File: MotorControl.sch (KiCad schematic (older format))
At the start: 0 parts

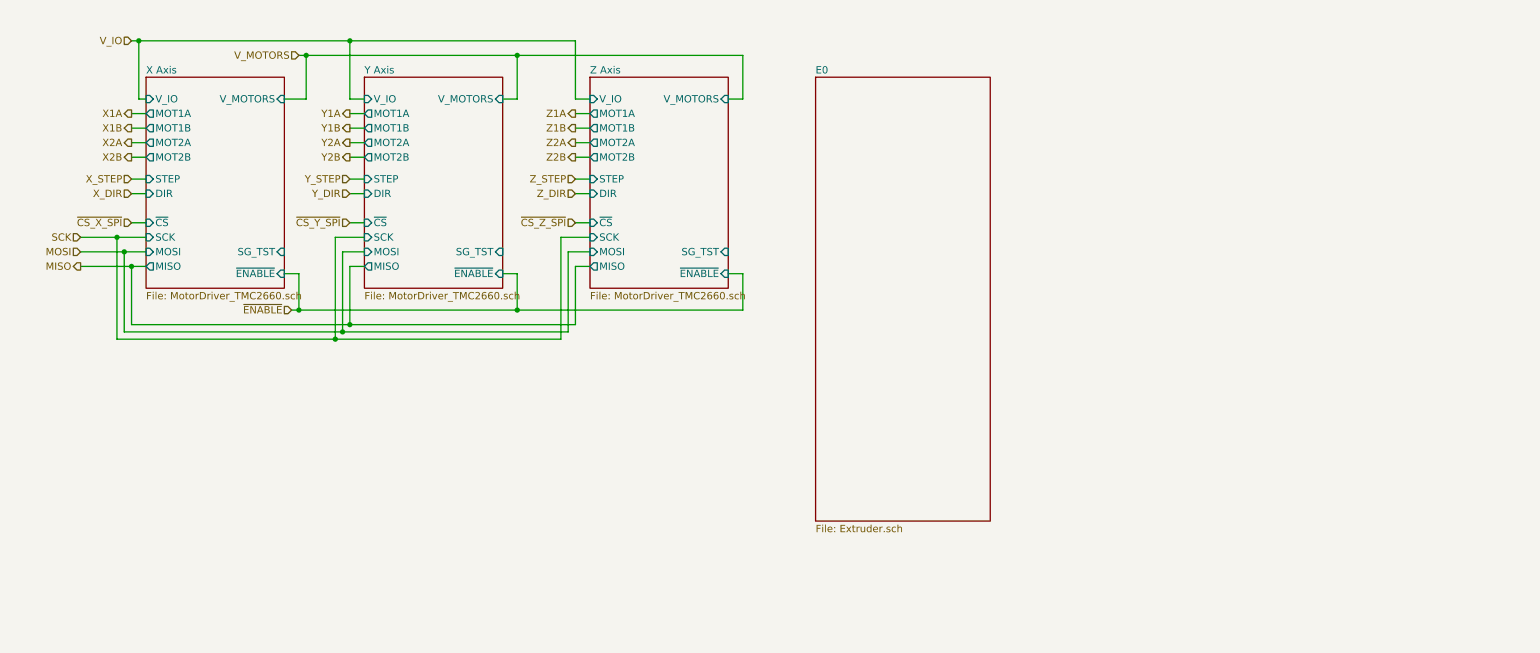
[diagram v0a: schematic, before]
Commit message: Add 3 axis and 2 extruders. Basic thermistor temperature sensing and MOSFET heaters in the extruders.
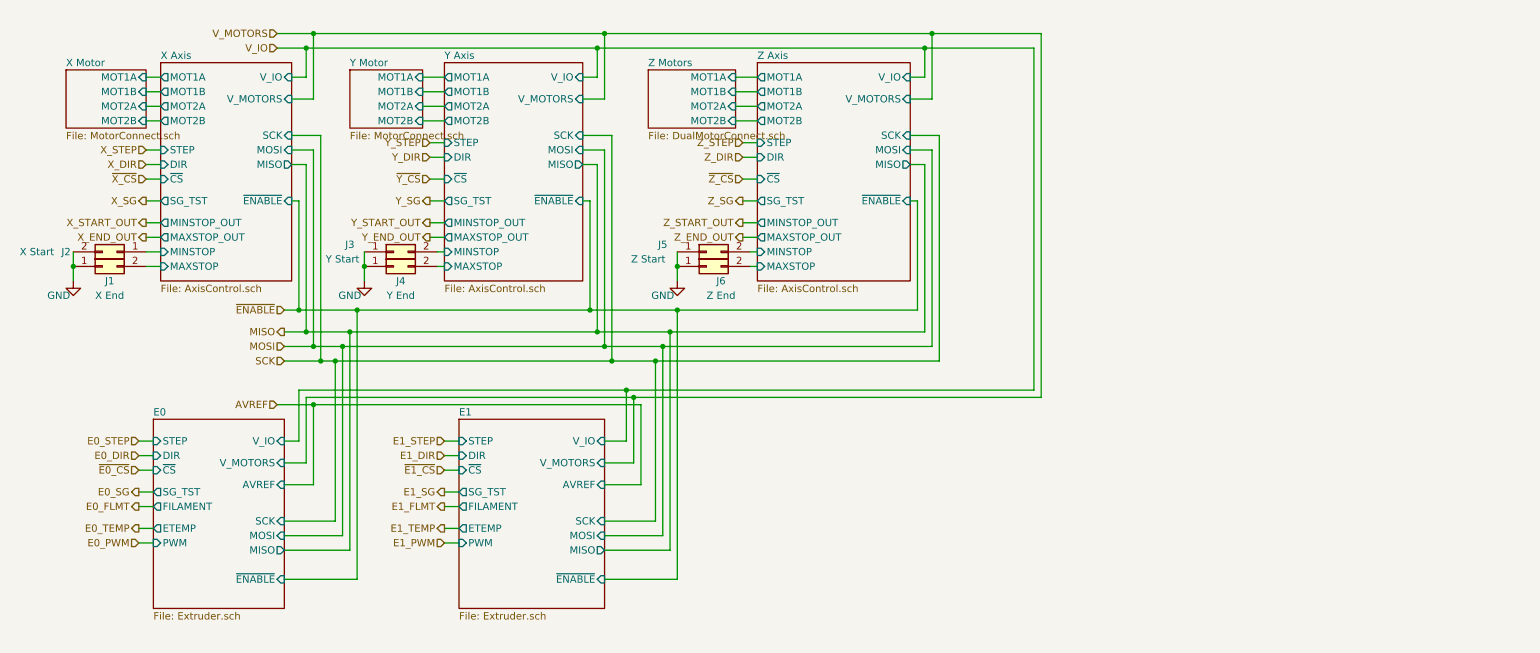
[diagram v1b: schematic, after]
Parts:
- added J1: X End, symbol Connector_Generic:Conn_02x01
- added J2: X Start, symbol Connector_Generic:Conn_02x01
- added J3: Y Start, symbol Connector_Generic:Conn_02x01
- added J4: Y End, symbol Connector_Generic:Conn_02x01
- added J5: Z Start, symbol Connector_Generic:Conn_02x01
- added J6: Z End, symbol Connector_Generic:Conn_02x01
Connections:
- new net GND: J1.1 (Pin_1), J2.2 (Pin_2), J3.1 (Pin_1), J4.1 (Pin_1), J5.1 (Pin_1), J6.1 (Pin_1)
- new net X Axis/MAXSTOP: J1.2 (Pin_2)
- new net X Axis/MINSTOP: J2.1 (Pin_1)
- new net Y Axis/MAXSTOP: J4.2 (Pin_2)
- new net Y Axis/MINSTOP: J3.2 (Pin_2)
- new net Z Axis/MAXSTOP: J6.2 (Pin_2)
- new net Z Axis/MINSTOP: J5.2 (Pin_2)

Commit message: Added the rest of the printer parts. Should be complete more or less.
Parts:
- removed J1: X End, symbol Connector_Generic:Conn_02x01
- removed J2: X Start, symbol Connector_Generic:Conn_02x01
- removed J3: Y Start, symbol Connector_Generic:Conn_02x01
- removed J4: Y End, symbol Connector_Generic:Conn_02x01
- removed J5: Z Start, symbol Connector_Generic:Conn_02x01
- removed J6: Z End, symbol Connector_Generic:Conn_02x01
- added C?: 0.1uF, symbol Device:C
- added U? (x5): 74LVC125, symbol Logic_74xx:74LVC125
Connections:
- net GND: now also C?.2, U?.1, U?.10, U?.13, U?.4, U?.7 (GND)
- net MISO: now also U?.11
- net MOSI: now also U?.5
- net SCK: now also U?.9
- net V_IO: now also C?.1, U?.14 (VCC)
- net ~ENABLE: now also U?.2
- new net E0/MISO: U?.12
- new net E0/MOSI: U?.6
- new net E0/SCK: U?.8
- new net E0/~ENABLE: U?.3

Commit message: Finish the schematics. All pins are assinged to the NUCLEO-64 board.
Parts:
- gave numbers to parts that had none: 2
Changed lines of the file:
@@
 	5450 3900 5350 3900
 $Comp
-L Logic_74xx:74LVC125 U?
+L Logic_74xx:74LVC125 U3
 U 1 1 5ABD1500
 P 3600 2900
-F 0 "U?" H 3650 3050 50  0000 C CNN
+F 0 "U3" H 3650 3050 50  0000 C CNN
 F 1 "74LVC125" H 3200 3000 50  0000 C CNN
 F 2 "" H 3600 2900 50  0001 C CNN
@@
 $EndComp
 $Comp
-L Logic_74xx:74LVC125 U?
+L Logic_74xx:74LVC125 U3
 U 3 1 5ABD166B
 P 2900 3550
-F 0 "U?" H 2750 3350 50  0000 C CNN
+F 0 "U3" H 2750 3350 50  0000 C CNN
 F 1 "74LVC125" H 2550 3450 50  0000 C CNN
 F 2 "" H 2900 3550 50  0001 C CNN
@@
 	3250 3800 2900 3800
 $Comp
-L power:GND #PWR?
+L power:GND #PWR08
 U 1 1 5AC17846
 P 2700 3900
-F 0 "#PWR?" H 2700 3650 50  0001 C CNN
+F 0 "#PWR08" H 2700 3650 50  0001 C CNN
 F 1 "GND" H 2705 3727 50  0000 C CNN
 F 2 "" H 2700 3900 50  0001 C CNN
@@
 Connection ~ 2900 3800
 $Comp
-L Logic_74xx:74LVC125 U?
+L Logic_74xx:74LVC125 U3
 U 2 1 5ABD15E4
 P 3250 3200
-F 0 "U?" H 3250 3400 50  0000 C CNN
+F 0 "U3" H 3250 3400 50  0000 C CNN
 F 1 "74LVC125" H 2900 3350 50  0000 C CNN
 F 2 "" H 3250 3200 50  0001 C CNN
@@
 	2550 3200 2950 3200
 $Comp
-L Logic_74xx:74LVC125 U?
+L Logic_74xx:74LVC125 U3
 U 4 1 5AC4CBF3
 P 9100 3150
-F 0 "U?" H 9100 3467 50  0000 C CNN
+F 0 "U3" H 9100 3467 50  0000 C CNN
 F 1 "74LVC125" H 9100 3376 50  0000 C CNN
 F 2 "" H 9100 3150 50  0001 C CNN
@@
 	9400 3150 9950 3150
 $Comp
-L power:GND #PWR?
+L power:GND #PWR010
 U 1 1 5AC6FCE8
 P 9200 3400
-F 0 "#PWR?" H 9200 3150 50  0001 C CNN
+F 0 "#PWR010" H 9200 3150 50  0001 C CNN
 F 1 "GND" H 9350 3350 50  0000 C CNN
 F 2 "" H 9200 3400 50  0001 C CNN
@@
 	9100 3400 9200 3400
 $Comp
-L Logic_74xx:74LVC125 U?
+L Logic_74xx:74LVC125 U3
 U 5 1 5AC78AD7
 P 8700 4350
-F 0 "U?" H 8930 4396 50  0000 L CNN
+F 0 "U3" H 8930 4396 50  0000 L CNN
 F 1 "74LVC125" H 8930 4305 50  0000 L CNN
 F 2 "" H 8700 4350 50  0001 C CNN
@@
 	8700 3550 9550 3550
 $Comp
-L power:GND #PWR?
+L power:GND #PWR09
 U 1 1 5AC8199D
 P 8700 4950
-F 0 "#PWR?" H 8700 4700 50  0001 C CNN
+F 0 "#PWR09" H 8700 4700 50  0001 C CNN
 F 1 "GND" H 8705 4777 50  0000 C CNN
 F 2 "" H 8700 4950 50  0001 C CNN
@@
 $EndComp
 $Comp
-L Device:C C?
+L Device:C C3
 U 1 1 5AC819E3
 P 8100 4300
-F 0 "C?" H 8215 4346 50  0000 L CNN
+F 0 "C3" H 8215 4346 50  0000 L CNN
 F 1 "0.1uF" H 8215 4255 50  0000 L CNN
 F 2 "" H 8138 4150 50  0001 C CNN

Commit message: Assigned footprints for all components. Inductors are approximate size. MOSFETs dont agree with the footprints. Saved pcb netlist report as report.txt.
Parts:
- C3: footprint (none) -> Capacitor_SMD:C_0603_1608Metric
- U3: footprint (none) -> Package_SO:TSSOP-16-1EP_4.4x5mm_P0.65mm
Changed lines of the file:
@@
 F 0 "U3" H 3650 3050 50  0000 C CNN
 F 1 "74LVC125" H 3200 3000 50  0000 C CNN
-F 2 "" H 3600 2900 50  0001 C CNN
+F 2 "Package_SO:TSSOP-16-1EP_4.4x5mm_P0.65mm" H 3600 2900 50  0001 C CNN
 F 3 "http://www.ti.com/lit/gpn/sn74LVC125" H 3600 2900 50  0001 C CNN
 	1    3600 2900
@@
 F 0 "U3" H 2750 3350 50  0000 C CNN
 F 1 "74LVC125" H 2550 3450 50  0000 C CNN
-F 2 "" H 2900 3550 50  0001 C CNN
+F 2 "Package_SO:TSSOP-16-1EP_4.4x5mm_P0.65mm" H 2900 3550 50  0001 C CNN
 F 3 "http://www.ti.com/lit/gpn/sn74LVC125" H 2900 3550 50  0001 C CNN
 	3    2900 3550
@@
 F 0 "U3" H 3250 3400 50  0000 C CNN
 F 1 "74LVC125" H 2900 3350 50  0000 C CNN
-F 2 "" H 3250 3200 50  0001 C CNN
+F 2 "Package_SO:TSSOP-16-1EP_4.4x5mm_P0.65mm" H 3250 3200 50  0001 C CNN
 F 3 "http://www.ti.com/lit/gpn/sn74LVC125" H 3250 3200 50  0001 C CNN
 	2    3250 3200
@@
 F 0 "U3" H 9100 3467 50  0000 C CNN
 F 1 "74LVC125" H 9100 3376 50  0000 C CNN
-F 2 "" H 9100 3150 50  0001 C CNN
+F 2 "Package_SO:TSSOP-16-1EP_4.4x5mm_P0.65mm" H 9100 3150 50  0001 C CNN
 F 3 "http://www.ti.com/lit/gpn/sn74LVC125" H 9100 3150 50  0001 C CNN
 	4    9100 3150
@@
 F 0 "U3" H 8930 4396 50  0000 L CNN
 F 1 "74LVC125" H 8930 4305 50  0000 L CNN
-F 2 "" H 8700 4350 50  0001 C CNN
+F 2 "Package_SO:TSSOP-16-1EP_4.4x5mm_P0.65mm" H 8700 4350 50  0001 C CNN
 F 3 "http://www.ti.com/lit/gpn/sn74LVC125" H 8700 4350 50  0001 C CNN
 	5    8700 4350
@@
 F 0 "C3" H 8215 4346 50  0000 L CNN
 F 1 "0.1uF" H 8215 4255 50  0000 L CNN
-F 2 "" H 8138 4150 50  0001 C CNN
+F 2 "Capacitor_SMD:C_0603_1608Metric" H 8138 4150 50  0001 C CNN
 F 3 "~" H 8100 4300 50  0001 C CNN
 	1    8100 4300

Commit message: Updated components. Removed power supply. Component layout on PCB.
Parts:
- U3: footprint Package_SO:TSSOP-16-1EP_4.4x5mm_P0.65mm -> Package_SO:TSSOP-14-1EP_4.4x5mm_P0.65mm
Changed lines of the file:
@@
 $Descr A4 11693 8268
 encoding utf-8
-Sheet 2 35
+Sheet 2 34
 Title ""
 Date ""
@@
 F 0 "U3" H 3650 3050 50  0000 C CNN
 F 1 "74LVC125" H 3200 3000 50  0000 C CNN
-F 2 "Package_SO:TSSOP-16-1EP_4.4x5mm_P0.65mm" H 3600 2900 50  0001 C CNN
+F 2 "Package_SO:TSSOP-14-1EP_4.4x5mm_P0.65mm" H 3600 2900 50  0001 C CNN
 F 3 "http://www.ti.com/lit/gpn/sn74LVC125" H 3600 2900 50  0001 C CNN
 	1    3600 2900
@@
 F 0 "U3" H 2750 3350 50  0000 C CNN
 F 1 "74LVC125" H 2550 3450 50  0000 C CNN
-F 2 "Package_SO:TSSOP-16-1EP_4.4x5mm_P0.65mm" H 2900 3550 50  0001 C CNN
+F 2 "Package_SO:TSSOP-14-1EP_4.4x5mm_P0.65mm" H 2900 3550 50  0001 C CNN
 F 3 "http://www.ti.com/lit/gpn/sn74LVC125" H 2900 3550 50  0001 C CNN
 	3    2900 3550
@@
 F 0 "U3" H 3250 3400 50  0000 C CNN
 F 1 "74LVC125" H 2900 3350 50  0000 C CNN
-F 2 "Package_SO:TSSOP-16-1EP_4.4x5mm_P0.65mm" H 3250 3200 50  0001 C CNN
+F 2 "Package_SO:TSSOP-14-1EP_4.4x5mm_P0.65mm" H 3250 3200 50  0001 C CNN
 F 3 "http://www.ti.com/lit/gpn/sn74LVC125" H 3250 3200 50  0001 C CNN
 	2    3250 3200
@@
 F 0 "U3" H 9100 3467 50  0000 C CNN
 F 1 "74LVC125" H 9100 3376 50  0000 C CNN
-F 2 "Package_SO:TSSOP-16-1EP_4.4x5mm_P0.65mm" H 9100 3150 50  0001 C CNN
+F 2 "Package_SO:TSSOP-14-1EP_4.4x5mm_P0.65mm" H 9100 3150 50  0001 C CNN
 F 3 "http://www.ti.com/lit/gpn/sn74LVC125" H 9100 3150 50  0001 C CNN
 	4    9100 3150
@@
 F 0 "U3" H 8930 4396 50  0000 L CNN
 F 1 "74LVC125" H 8930 4305 50  0000 L CNN
-F 2 "Package_SO:TSSOP-16-1EP_4.4x5mm_P0.65mm" H 8700 4350 50  0001 C CNN
+F 2 "Package_SO:TSSOP-14-1EP_4.4x5mm_P0.65mm" H 8700 4350 50  0001 C CNN
 F 3 "http://www.ti.com/lit/gpn/sn74LVC125" H 8700 4350 50  0001 C CNN
 	5    8700 4350

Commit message: Added mounting holes and fiducials. Placed all components labels so they are readable.
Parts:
- U3: footprint Package_SO:TSSOP-14-1EP_4.4x5mm_P0.65mm -> Package_SO:TSSOP-14_4.4x5mm_P0.65mm
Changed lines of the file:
@@
 F 0 "U3" H 3650 3050 50  0000 C CNN
 F 1 "74LVC125" H 3200 3000 50  0000 C CNN
-F 2 "Package_SO:TSSOP-14-1EP_4.4x5mm_P0.65mm" H 3600 2900 50  0001 C CNN
+F 2 "Package_SO:TSSOP-14_4.4x5mm_P0.65mm" H 3600 2900 50  0001 C CNN
 F 3 "http://www.ti.com/lit/gpn/sn74LVC125" H 3600 2900 50  0001 C CNN
 	1    3600 2900
@@
 F 0 "U3" H 2750 3350 50  0000 C CNN
 F 1 "74LVC125" H 2550 3450 50  0000 C CNN
-F 2 "Package_SO:TSSOP-14-1EP_4.4x5mm_P0.65mm" H 2900 3550 50  0001 C CNN
+F 2 "Package_SO:TSSOP-14_4.4x5mm_P0.65mm" H 2900 3550 50  0001 C CNN
 F 3 "http://www.ti.com/lit/gpn/sn74LVC125" H 2900 3550 50  0001 C CNN
 	3    2900 3550
@@
 F 0 "U3" H 3250 3400 50  0000 C CNN
 F 1 "74LVC125" H 2900 3350 50  0000 C CNN
-F 2 "Package_SO:TSSOP-14-1EP_4.4x5mm_P0.65mm" H 3250 3200 50  0001 C CNN
+F 2 "Package_SO:TSSOP-14_4.4x5mm_P0.65mm" H 3250 3200 50  0001 C CNN
 F 3 "http://www.ti.com/lit/gpn/sn74LVC125" H 3250 3200 50  0001 C CNN
 	2    3250 3200
@@
 F 0 "U3" H 9100 3467 50  0000 C CNN
 F 1 "74LVC125" H 9100 3376 50  0000 C CNN
-F 2 "Package_SO:TSSOP-14-1EP_4.4x5mm_P0.65mm" H 9100 3150 50  0001 C CNN
+F 2 "Package_SO:TSSOP-14_4.4x5mm_P0.65mm" H 9100 3150 50  0001 C CNN
 F 3 "http://www.ti.com/lit/gpn/sn74LVC125" H 9100 3150 50  0001 C CNN
 	4    9100 3150
@@
 F 0 "U3" H 8930 4396 50  0000 L CNN
 F 1 "74LVC125" H 8930 4305 50  0000 L CNN
-F 2 "Package_SO:TSSOP-14-1EP_4.4x5mm_P0.65mm" H 8700 4350 50  0001 C CNN
+F 2 "Package_SO:TSSOP-14_4.4x5mm_P0.65mm" H 8700 4350 50  0001 C CNN
 F 3 "http://www.ti.com/lit/gpn/sn74LVC125" H 8700 4350 50  0001 C CNN
 	5    8700 4350

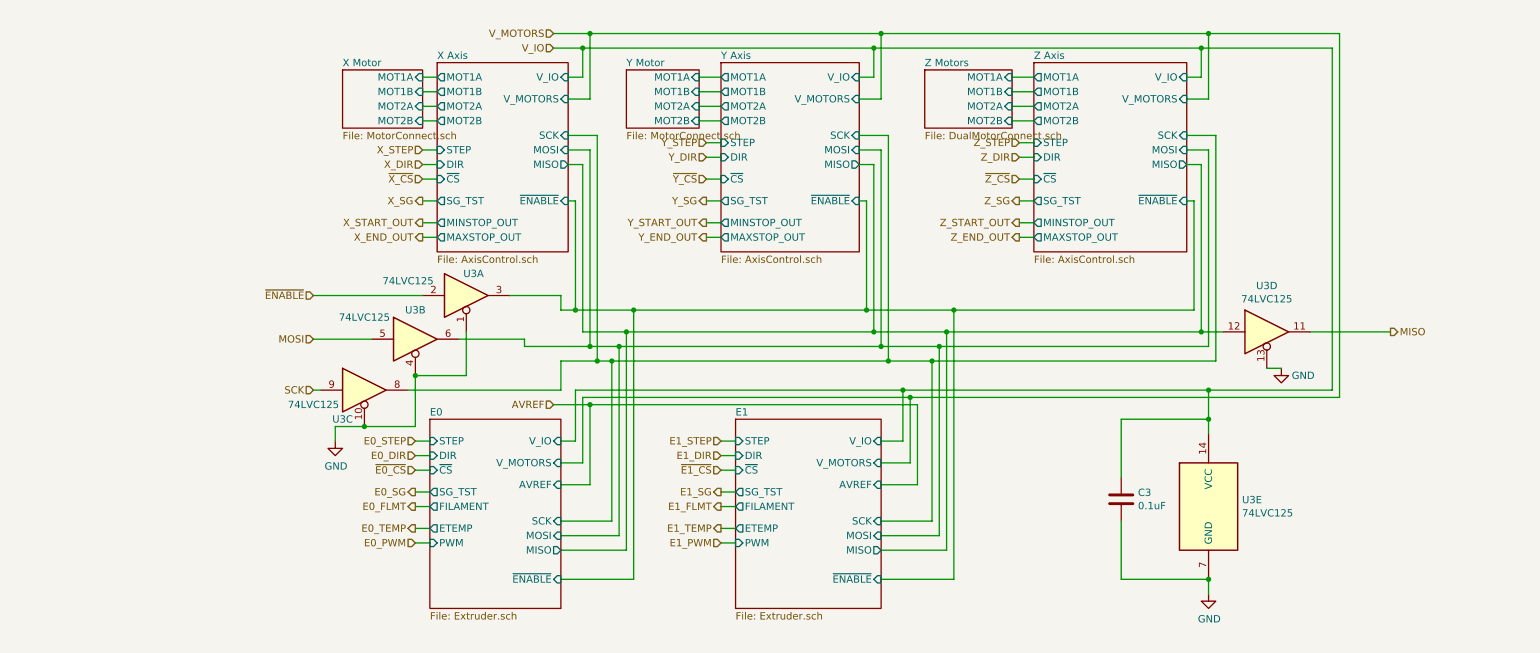
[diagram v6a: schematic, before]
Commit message: Update schematics to use TMC5130/TMC2130 drivers.
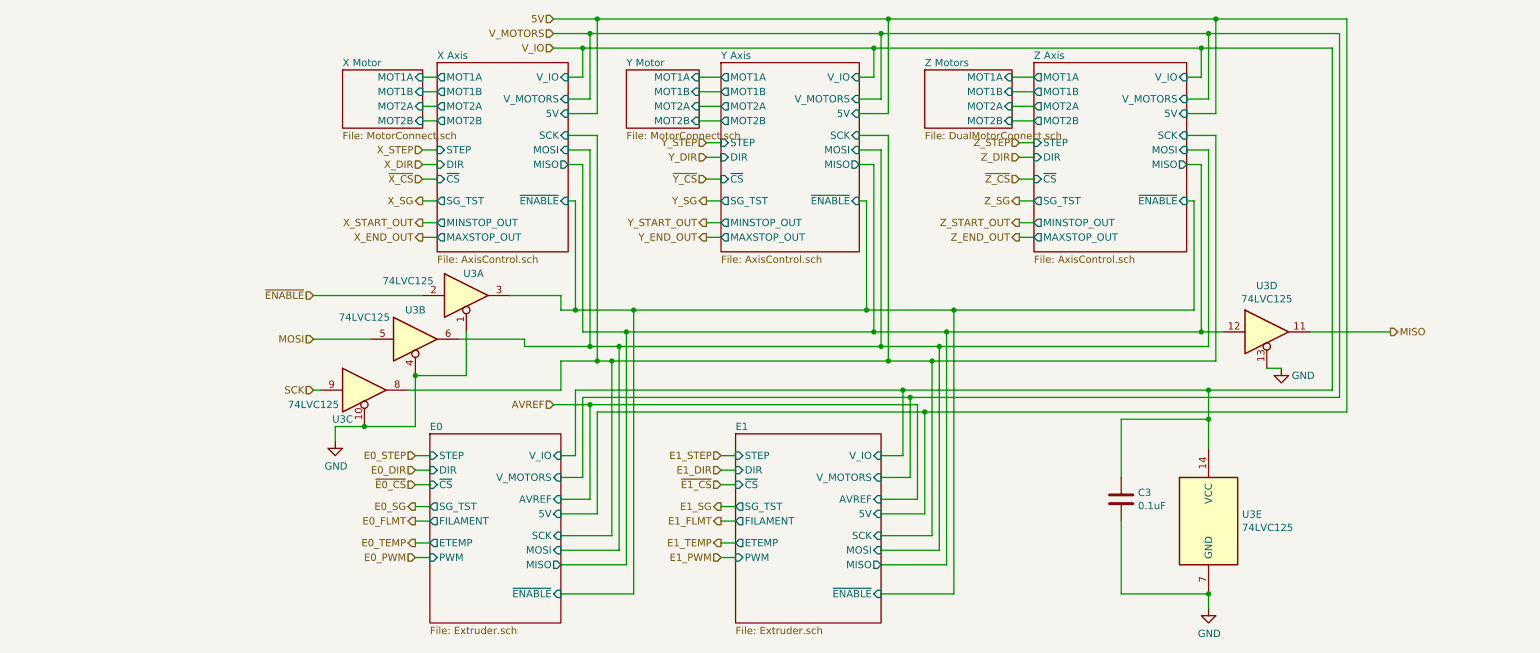
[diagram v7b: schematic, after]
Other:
- moved on the sheet: U3E
